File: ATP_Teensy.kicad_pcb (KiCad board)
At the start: 2 copper layers, 69.1 x 69.1 mm, 15 parts

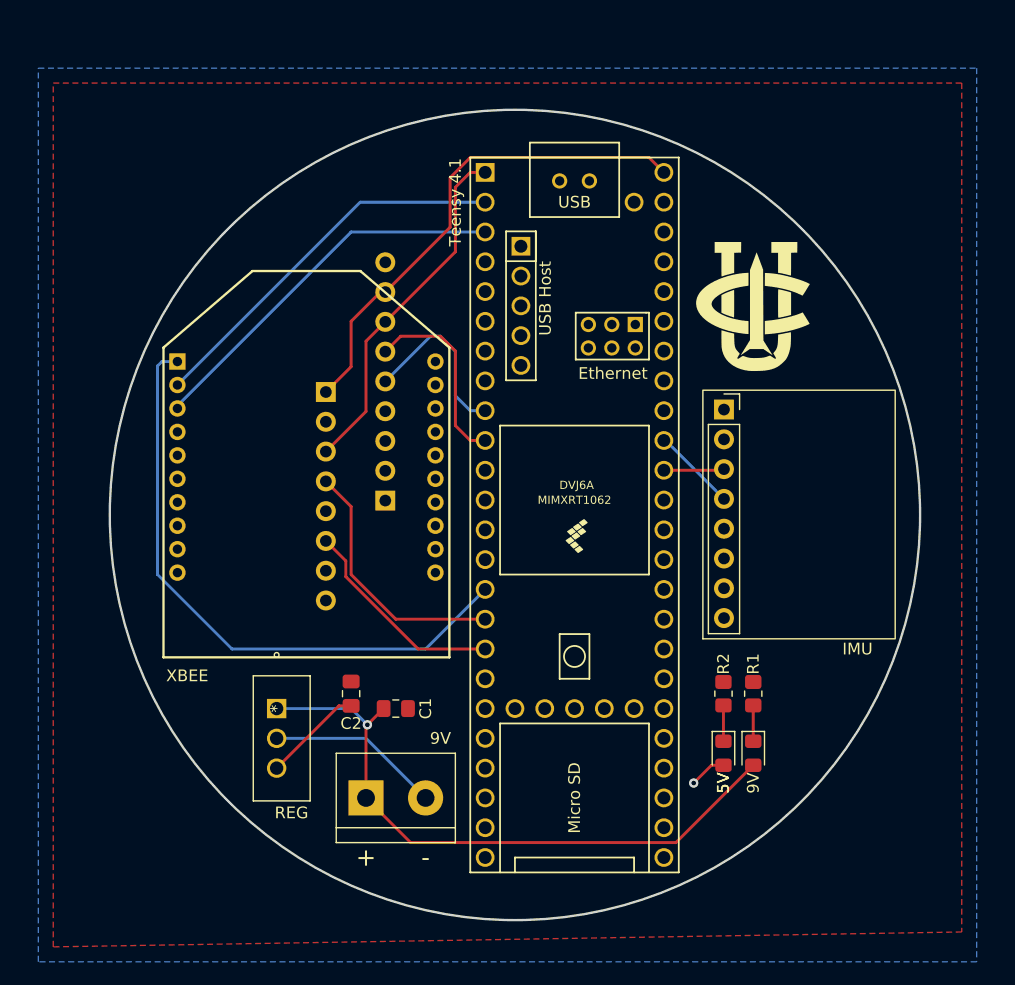
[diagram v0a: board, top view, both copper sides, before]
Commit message: Add mounting holes
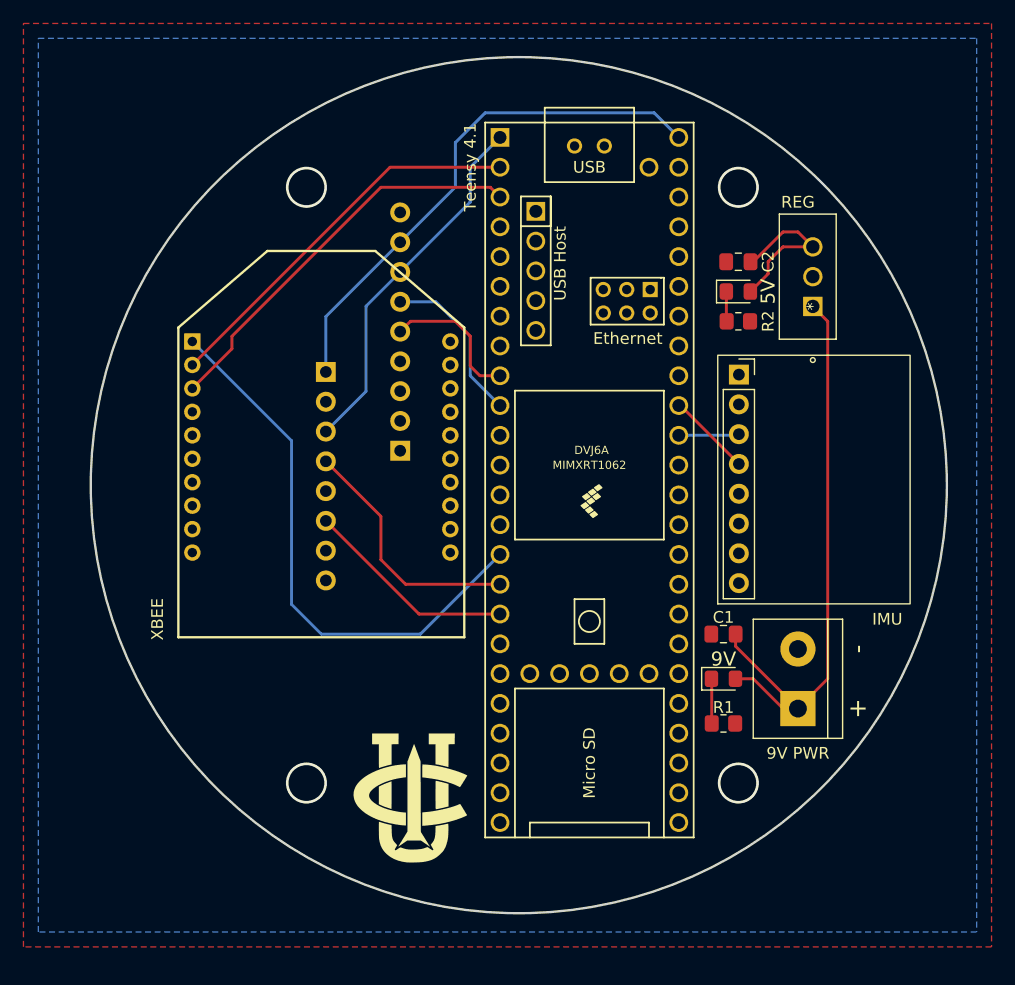
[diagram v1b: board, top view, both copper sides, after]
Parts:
- 9V PWR: renamed from 9V
- moved REG 57.1 mm to (177.8, 83.8), turned to 90 degrees
- moved Ge 51.1 mm to (143.5, 125.7)
- moved C2 49.5 mm to (171.4, 80.0), turned to 0 degrees
- moved Ge 44.5 mm to (144.0, 125.7)
- moved 5V 39.4 mm to (171.4, 82.5), turned to 0 degrees
- moved 9V PWR 37.6 mm to (176.5, 118.1), turned to 90 degrees
- moved R2 31.8 mm to (171.4, 85.1), turned to 0 degrees
- moved C1 28.7 mm to (170.2, 111.8), turned to 0 degrees
- moved 9V 6.84 mm to (170.2, 115.6), turned to 0 degrees
- moved GPS 4.44 mm to (140.1, 73.3)
- moved R1 3.59 mm to (170.2, 119.4), turned to 0 degrees
- moved Teensy 4.1 3.24 mm to (158.8, 98.6)
- moved IMU 3.24 mm to (169.7, 109.2)
- moved XBEE 2.13 mm to (135.9, 94.8)
- moved BMP 1.71 mm to (137.5, 109.4)
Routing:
- net GND: track 45.9 -> 31.2 mm
- net +5V: track 54.2 -> 59.5 mm, vias 1 -> 0
- net XBEE_VCC: track 52.3 -> 47.6 mm
- net +9V: track 55.2 -> 50.8 mm, vias 1 -> 0
- net GPS_TX: track 15.0 -> 12.3 mm
- net GPS_RX: track 16.5 -> 14.2 mm
- net XBEE_DIN: track 32.6 -> 34.3 mm
- net Net-(D1-Pad1): track 3.05 -> 3.86 mm
- net XBEE_DOUT: track 32.7 -> 33.2 mm
- net Net-(D2-Pad1): track 3.05 -> 2.55 mm
- net (no net): vias 0 -> 4
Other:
- board size 69.1 x 69.1 mm -> 73 x 73 mm

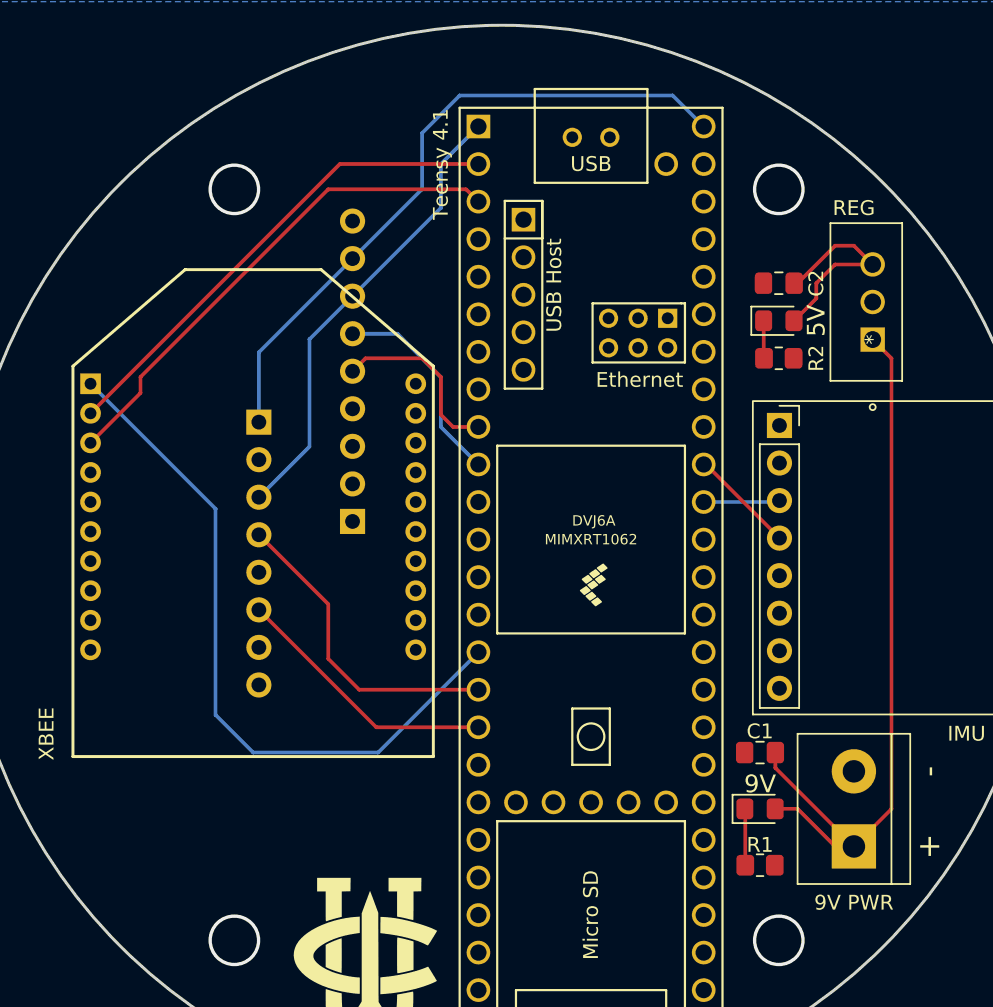
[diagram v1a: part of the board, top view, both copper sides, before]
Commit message: Change BMP connection from I2C to SPI
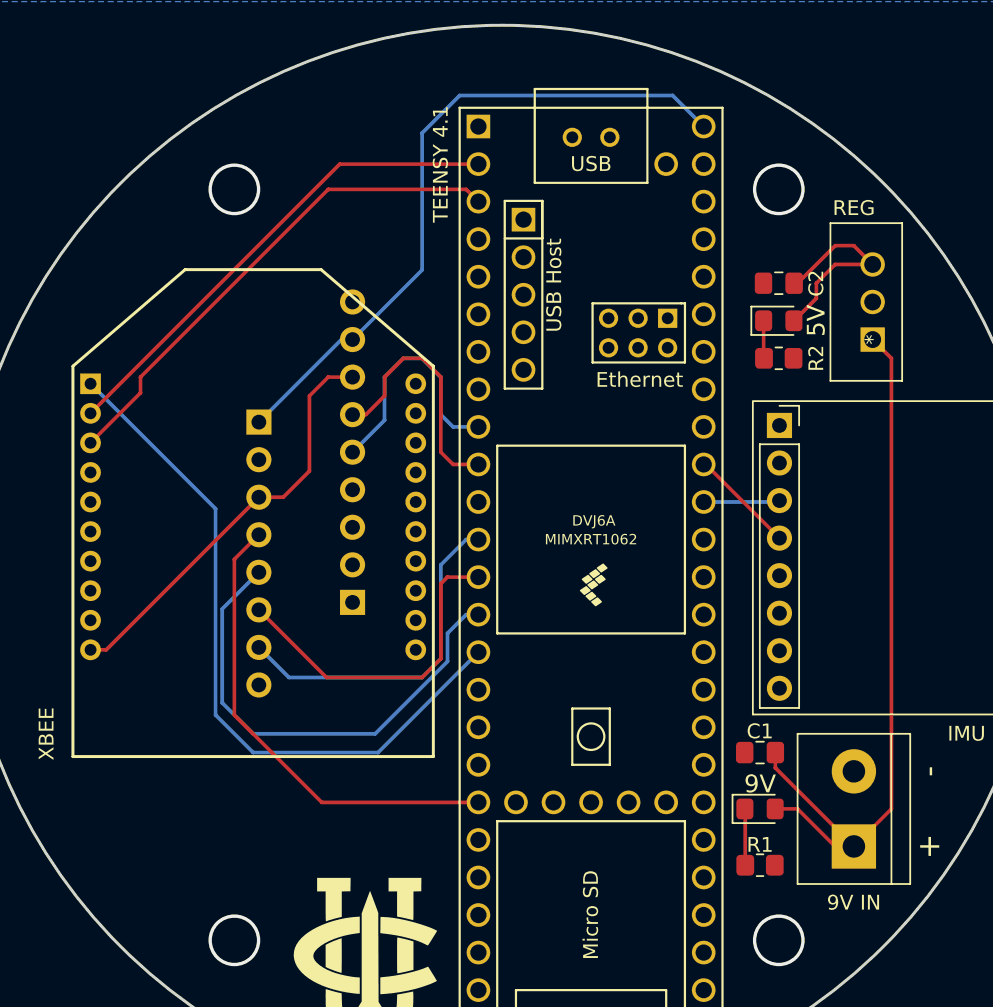
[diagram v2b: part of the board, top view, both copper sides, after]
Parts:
- 9V IN: renamed from 9V PWR
- REG: value L7805CV -> TO-220_STM
- TEENSY 4.1: renamed from Teensy 4.1
- moved GPS 5.47 mm to (140.1, 78.7)
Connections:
- BMP pad 5: unconnected-(U1-Pad5) -> BMP_SDO
- BMP pad 7: unconnected-(U1-Pad7) -> BMP_CS
- TEENSY 4.1 pad 12: unconnected-(U5-Pad12) -> BMP_CS
- TEENSY 4.1 pad 13: unconnected-(U5-Pad13) -> BMP_SDI
- TEENSY 4.1 pad 14: unconnected-(U5-Pad14) -> BMP_SDO
- TEENSY 4.1 pad 16: BMP_SCK -> unconnected-(U5-Pad16)
- TEENSY 4.1 pad 17: BMP_SDI -> unconnected-(U5-Pad17)
- TEENSY 4.1 pad 19: unconnected-(U5-Pad19) -> BMP_SCK
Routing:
- net BMP_SDO: track 0.00 -> 32.5 mm
- net BMP_CS: track 0.00 -> 23.3 mm
- net BMP_SCK: track 21.4 -> 32.5 mm
- net BMP_SDI: track 18.1 -> 22.5 mm
- net GPS_TX: track 12.3 -> 16.3 mm
- net GND: track 31.2 -> 28.3 mm
- net GPS_RX: track 14.2 -> 16.8 mm
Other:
- board text added: "UCI Rocket Project Avionics Flight Sensor"
- board text added: "v1.0 {dblquote}Rigel{dblquote} - DEC 2022 - Alexandra Z. J. https://github.com/UCI-Rocket-Project/AFS-PCB"
- board text removed: "November 2022 - Alexandra Z. J. https://github.com/UCI-Rocket-Project/ATP_Teensy4.1_VTF"
- board text removed: "UCI Rocket Project Avionics Test Payload"

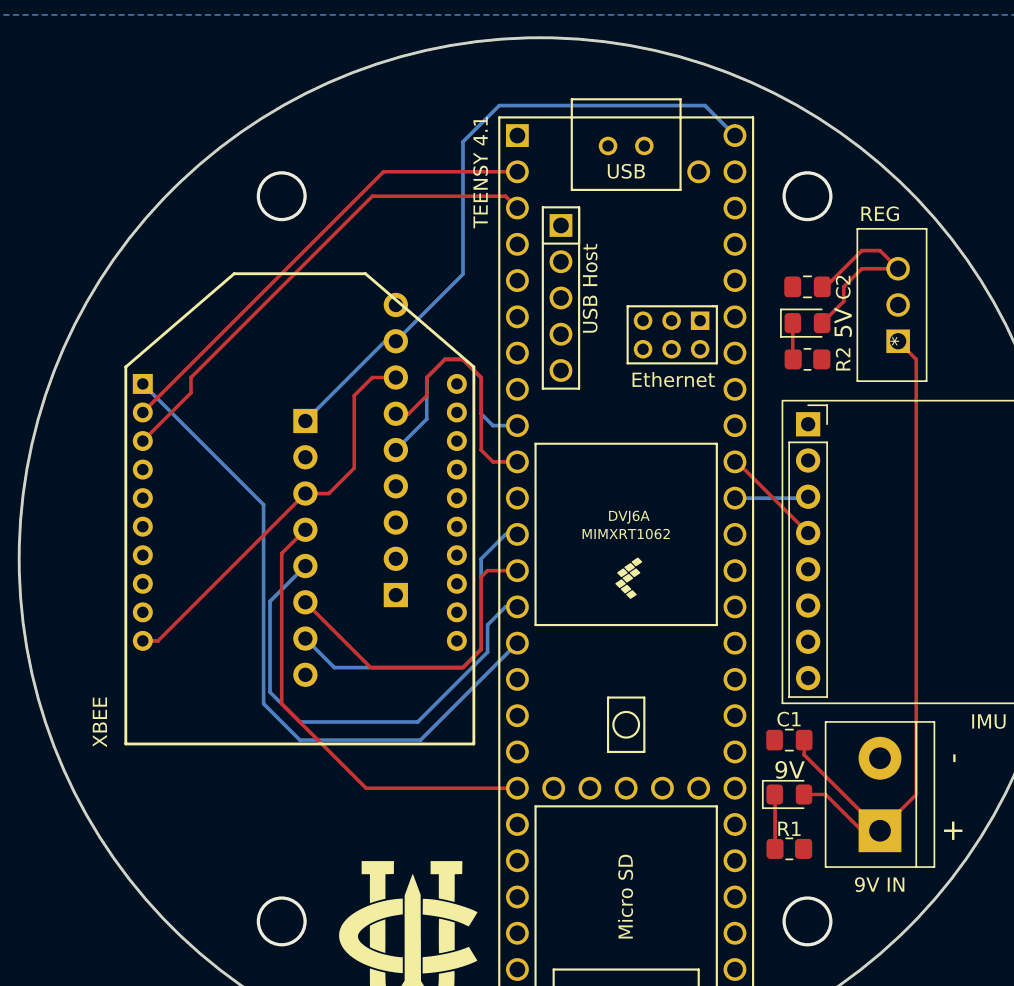
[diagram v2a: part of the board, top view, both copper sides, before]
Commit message: Add filtering capacitors for XBee
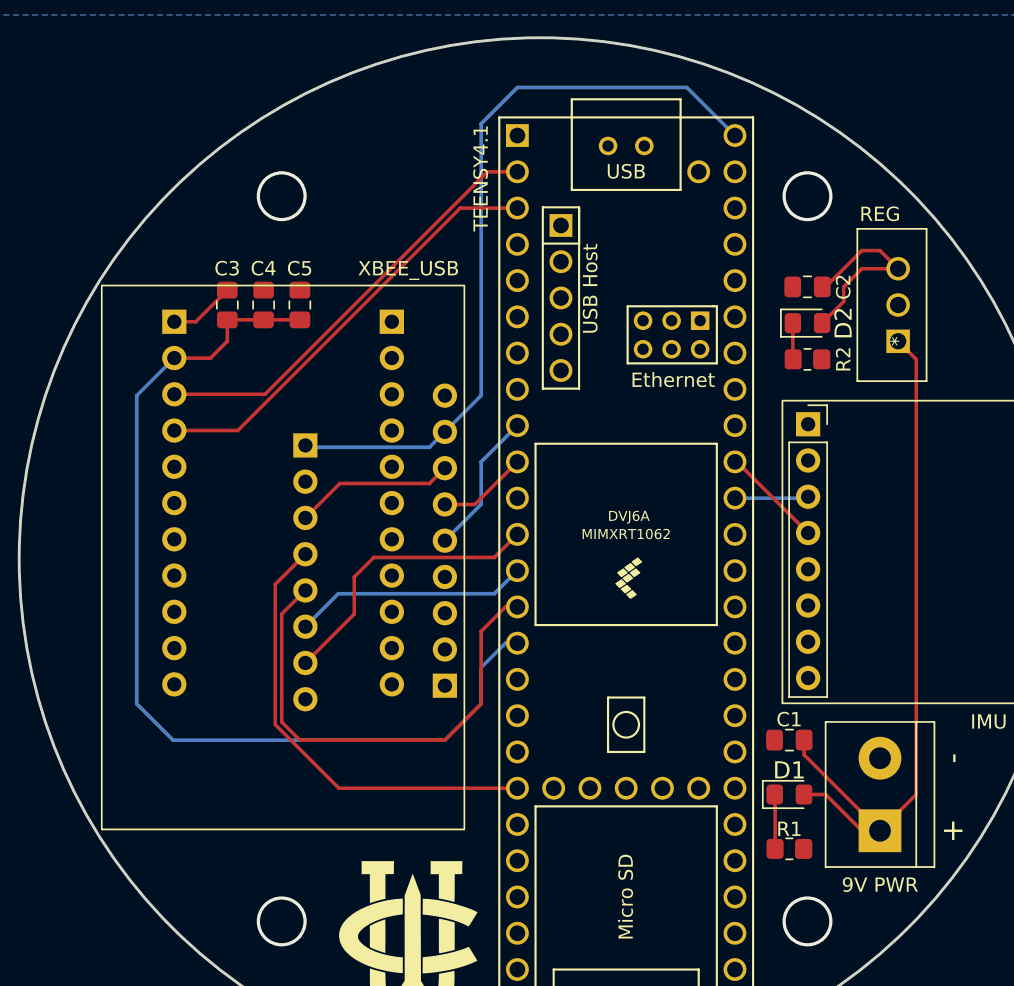
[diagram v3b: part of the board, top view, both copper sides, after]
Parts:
- removed XBEE: XBee_ProS3B, ATP_Teensy_footprints:XBEE_board
- added C3: 47pF, Capacitor_SMD:C_0805_2012Metric_Pad1.18x1.45mm_HandSolder, F.Cu at (130.8, 81.3)
- added C4: 1uF, Capacitor_SMD:C_0805_2012Metric_Pad1.18x1.45mm_HandSolder, F.Cu at (133.3, 81.3)
- added C5: 10uF, Capacitor_SMD:C_0805_2012Metric_Pad1.18x1.45mm_HandSolder, F.Cu at (135.9, 81.3)
- added XBEE_USB: FT231X_XBee_USB_Adapter, ATP_Teensy_footprints:XBee_Adapter, F.Cu at (122.0, 118.0)
- 9V PWR: renamed from 9V IN
- REG: value TO-220_STM -> L7805CV
- TEENSY4.1: renamed from TEENSY 4.1
- moved GPS 7.22 mm to (143.5, 85.1)
- moved BMP 1.71 mm to (137.5, 111.1)
- renumbered 9V to D1, 5V to D2
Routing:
- net XBEE_VCC: track 47.6 -> 68.1 mm
- net GND: track 28.3 -> 15.8 mm
- net GPS_RX: track 16.8 -> 6.31 mm
- net +5V: track 59.9 -> 67.5 mm
- net GPS_TX: track 16.3 -> 10.2 mm
- net BMP_SDI: track 22.5 -> 16.5 mm
- net XBEE_DIN: track 34.3 -> 30.5 mm
- net BMP_CS: track 23.3 -> 20.1 mm
- net XBEE_DOUT: track 33.2 -> 30.5 mm
- net BMP_SDO: track 32.5 -> 33.8 mm
- net BMP_SCK: track 32.5 -> 31.6 mm

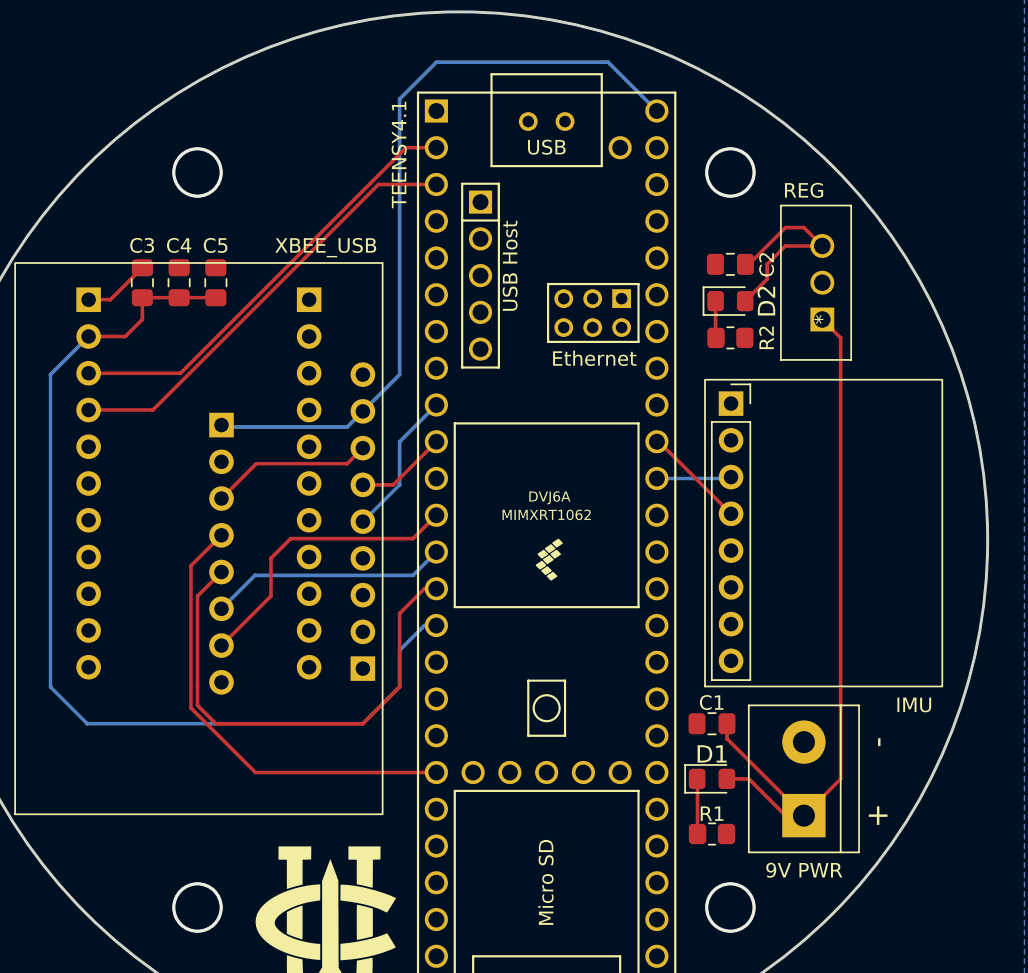
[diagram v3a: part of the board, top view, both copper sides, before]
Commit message: Replace 10uF CER CAP with 10uF ELE CAP
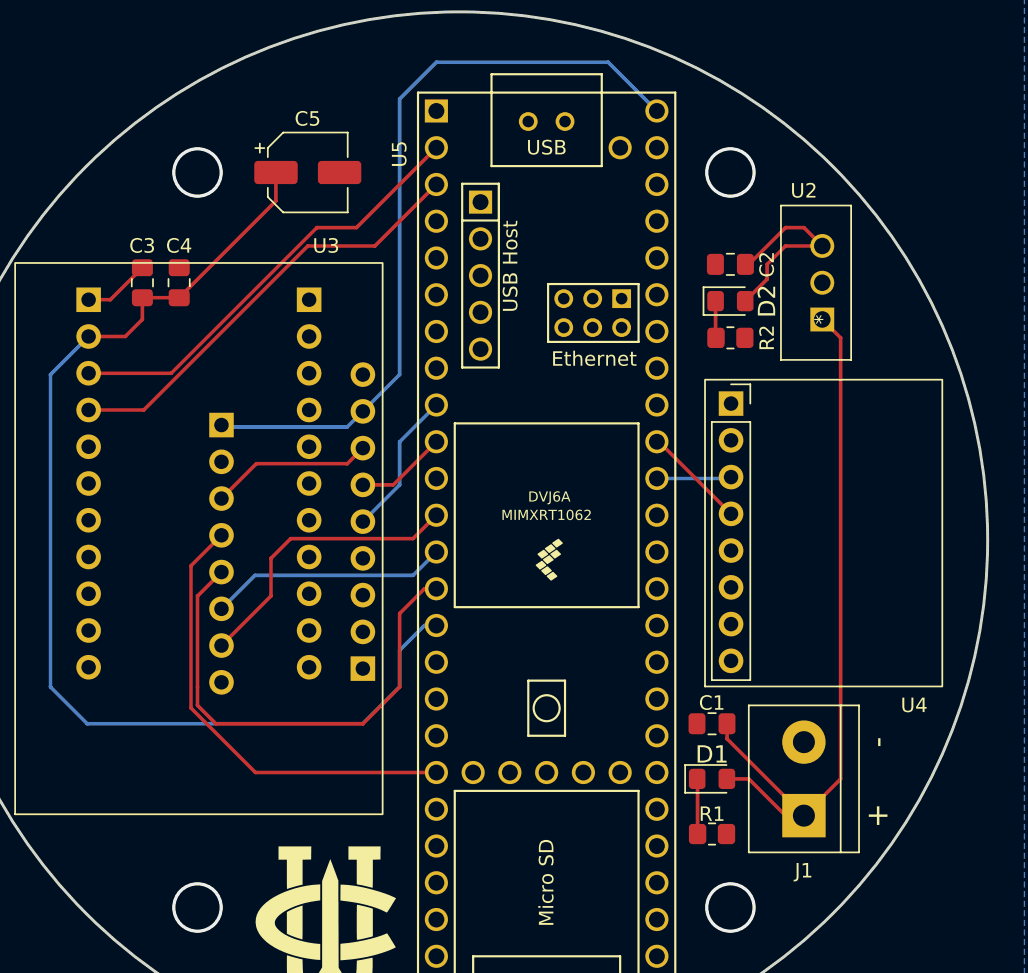
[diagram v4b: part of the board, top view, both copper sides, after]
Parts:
- C5: value 10uF -> 10uF, 50V; footprint Capacitor_SMD:C_0805_2012Metric_Pad1.18x1.45mm_HandSolder -> Capacitor_SMD:CP_Elec_5x5.4
- J1: renamed from 9V PWR
- moved C5 9.92 mm to (142.2, 73.7), turned to 0 degrees
- renumbered BMP to U1, REG to U2, XBEE_USB to U3, IMU to U4, TEENSY4.1 to U5, GPS to U6
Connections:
- C5 pad 1: GND -> XBEE_VCC
- C5 pad 2: XBEE_VCC -> GND
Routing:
- net XBEE_VCC: track 68.1 -> 77.0 mm
